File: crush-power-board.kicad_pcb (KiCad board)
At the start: 4 copper layers, 105 parts, among them J1 XT90PW-F, J2 1x2 Header, J3 Molex Micro Fit 3.0, J4 Barrel_Jack, J5 2157601008, U1 BD9G341AEFJ, U2 SIC461ED-T1-GE3, U3 SIC461ED-T1-GE3, U4 BD9G341AEFJ

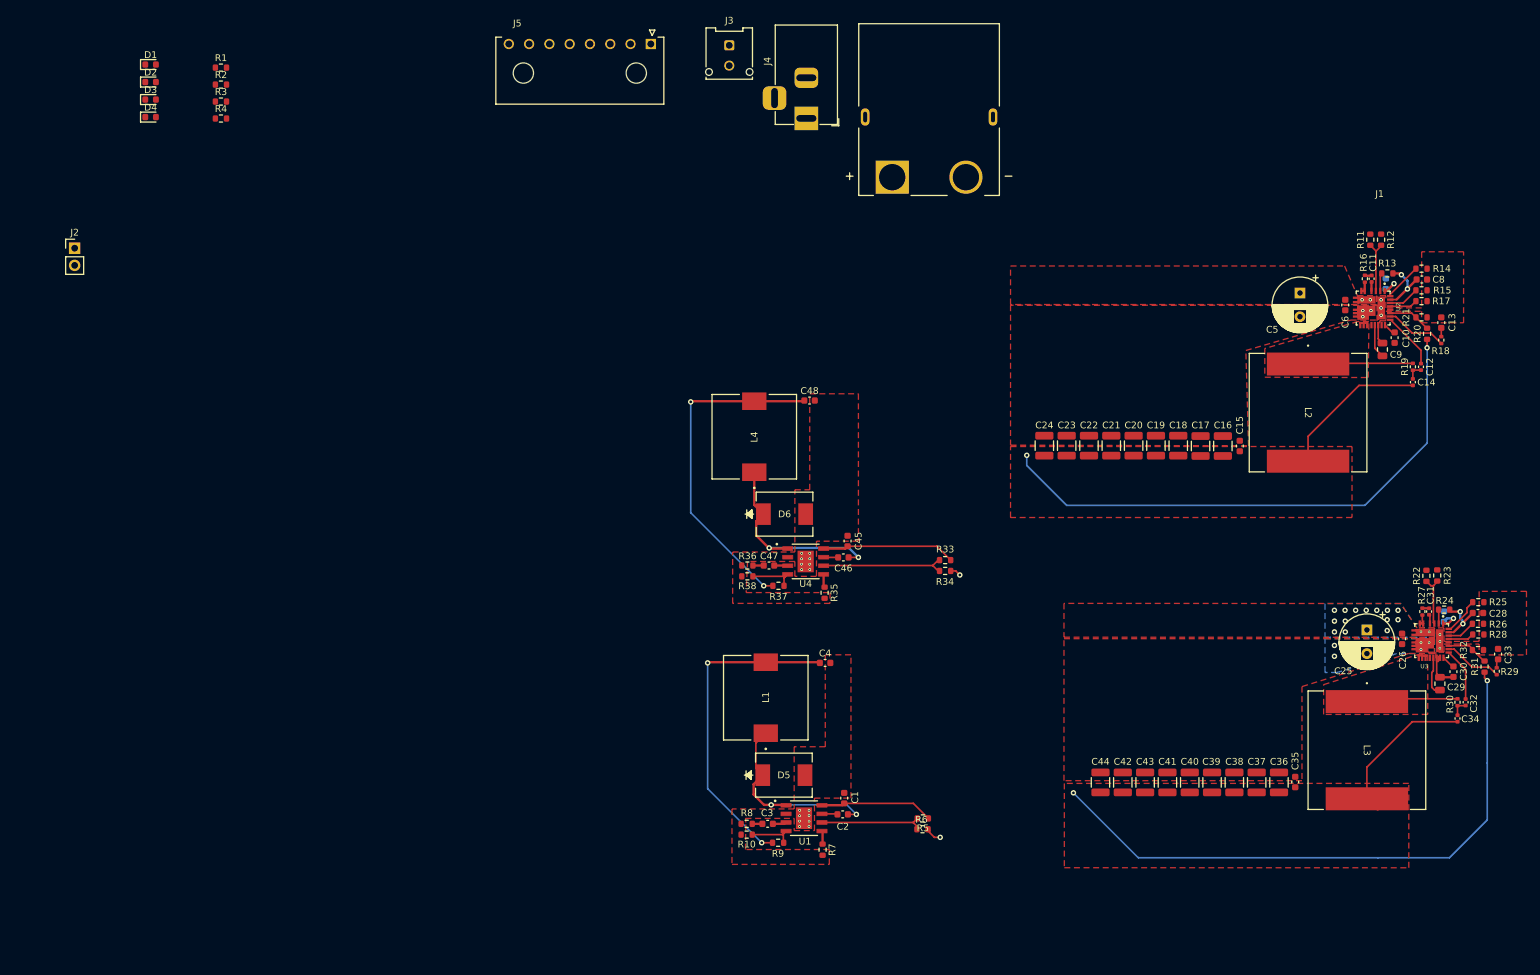
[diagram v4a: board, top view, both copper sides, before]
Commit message: fix drc violations
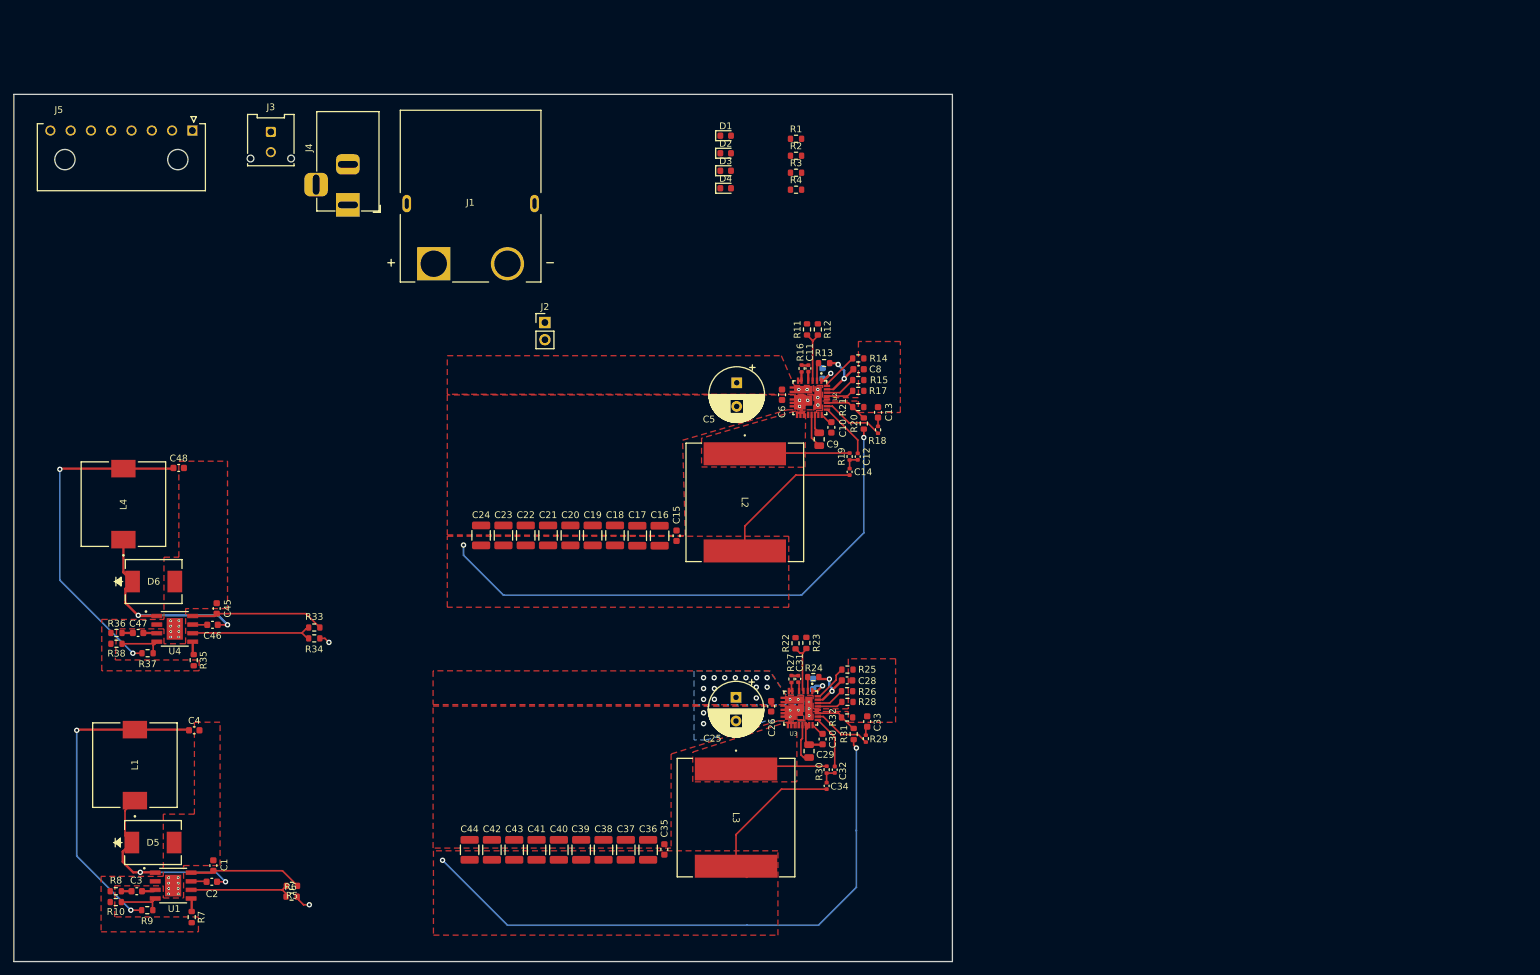
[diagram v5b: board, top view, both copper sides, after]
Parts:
- moved C2 93.8 mm to (71.0, 139.8)
- moved C25 93.8 mm to (148.5, 112.5)
- moved C26 93.8 mm to (153.7, 113.8)
- moved C28 93.8 mm to (164.9, 110.0)
- moved C3 93.8 mm to (59.9, 141.2)
- moved C31 93.8 mm to (157.7, 109.8)
- moved C36 93.8 mm to (135.5, 135.1)
- moved C37 93.8 mm to (132.2, 135.1)
- moved C39 93.8 mm to (125.6, 135.1)
- moved C4 93.8 mm to (68.4, 117.4)
- moved C41 93.8 mm to (119.0, 135.1)
- moved C44 93.8 mm to (109.1, 135.1)
- moved D6 93.8 mm to (62.4, 95.4)
- moved L1 93.8 mm to (59.6, 122.5)
- moved L3 93.8 mm to (148.5, 130.3)
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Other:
- board outline added: 138.8 x 128.2 mm

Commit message: preparing for board layout
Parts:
- moved R1 115.1 mm to (42.4, 33.4)
- moved R2 115.1 mm to (42.4, 35.9)
- moved R3 115.1 mm to (42.4, 38.4)
- moved R4 115.1 mm to (42.4, 40.9)
- moved D4 97.6 mm to (50.1, 25.8)
- moved D1 94.0 mm to (53.1, 33.2)
- moved D2 94.0 mm to (53.1, 35.8)
- moved D3 94.0 mm to (53.1, 38.4)
- moved C15 69.7 mm to (73.5, 66.8), turned to 0 degrees
- moved C16 68.1 mm to (73.5, 64.3), turned to 0 degrees
- moved J2 67.6 mm to (67.2, 15.2)
- moved C35 67.4 mm to (73.1, 116.7), turned to 0 degrees
- moved R22 66.7 mm to (92.7, 88.1), turned to 180 degrees
- moved C7 66.6 mm to (97.6, 45.1), turned to 0 degrees
- moved R23 66.6 mm to (95.0, 85.9)
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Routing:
- net 12V: track 104.6 -> 118.4 mm
- net 5V: track 112.9 -> 121.2 mm
- net Net-(U3-EN): track 7.77 -> 12.0 mm
- net GND1: track 1.60 -> 0.00 mm, vias 9 -> 8
- net +BATT: track 24.0 -> 25.3 mm
- net GND: track 10.7 -> 9.65 mm, vias 27 -> 92
- added copper zone on In2.Cu, net GND
- removed copper zone on B.Cu, net +BATT
- removed copper zone on B.Cu, net GND
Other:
- board size 138.8 x 128.2 mm -> 101.4 x 120.3 mm

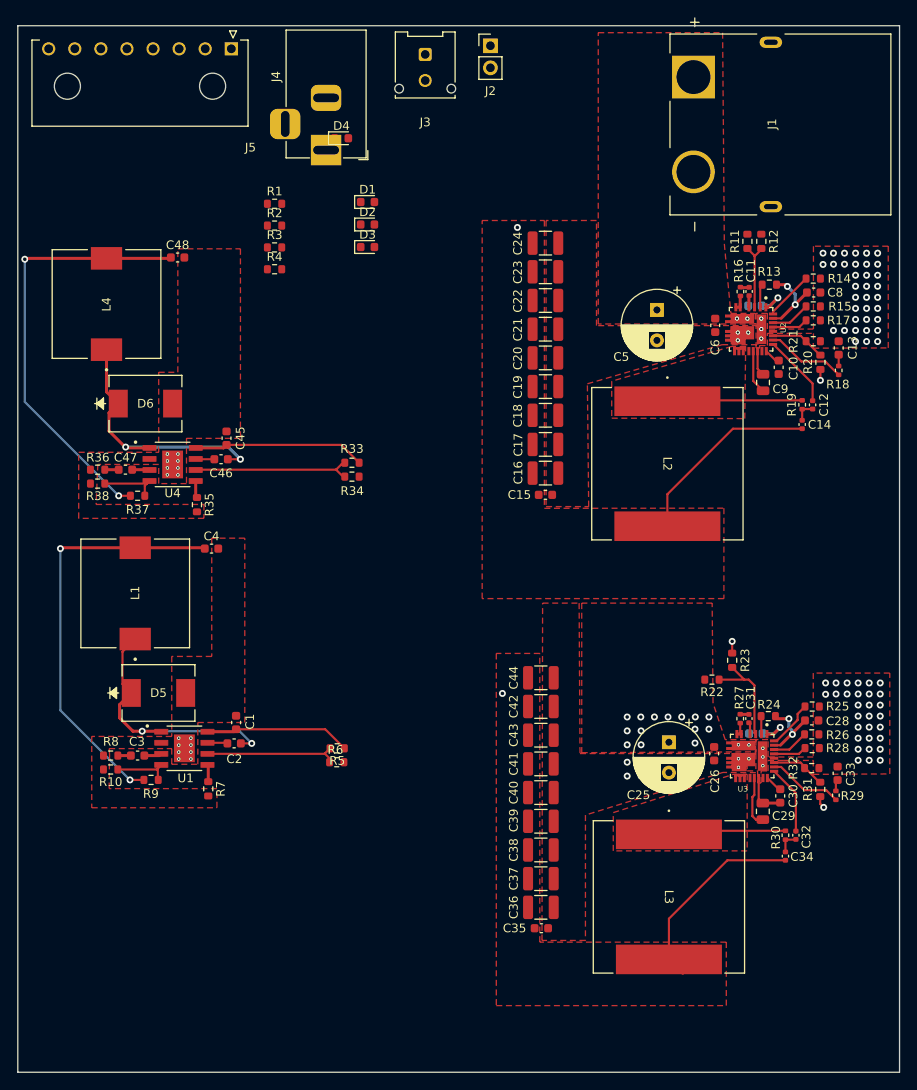
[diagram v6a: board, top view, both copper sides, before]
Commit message: layout majority of power board
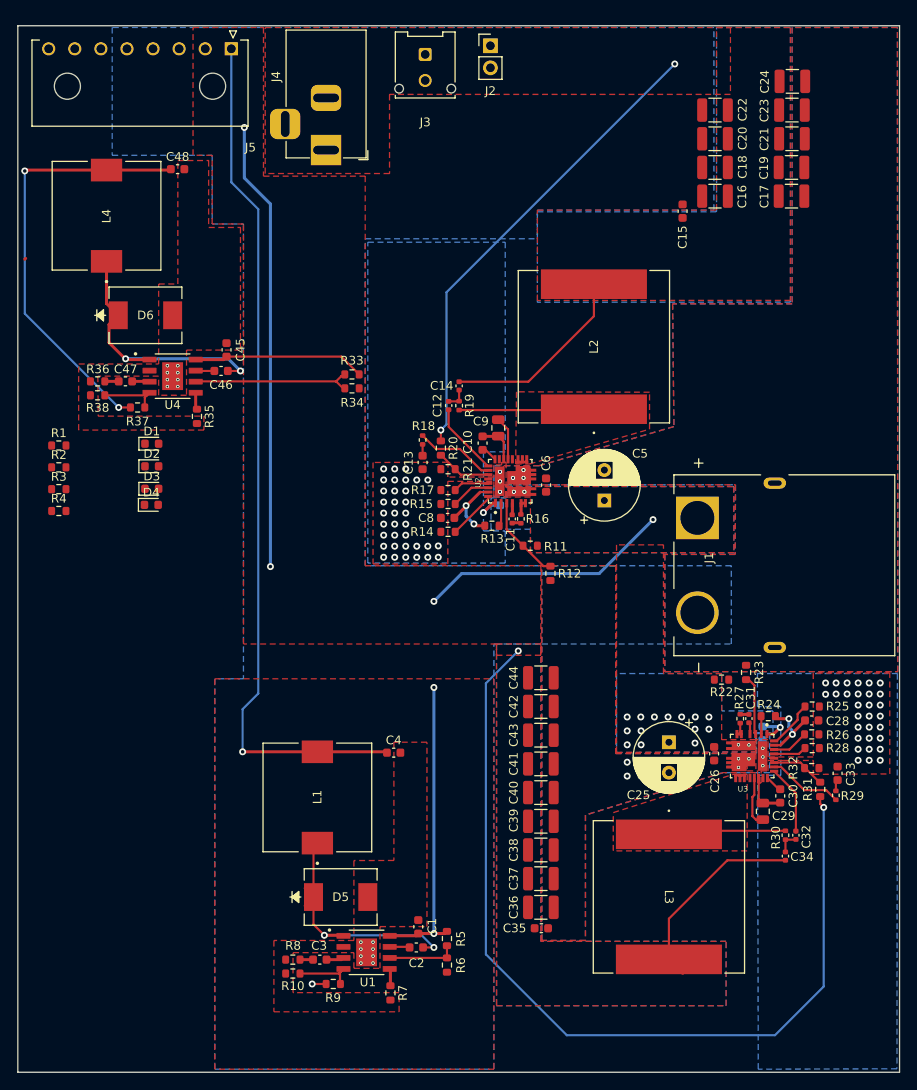
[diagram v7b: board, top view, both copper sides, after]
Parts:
- moved R14 51.1 mm to (62.3, 71.1), turned to 180 degrees
- moved J1 50.7 mm to (99.9, 75.0)
- moved C13 49.6 mm to (59.4, 63.1), turned to -90 degrees
- moved C8 49.4 mm to (62.3, 69.5), turned to 0 degrees
- moved R18 48.5 mm to (59.4, 60.5), turned to -90 degrees
- moved R15 47.8 mm to (62.3, 67.9), turned to 180 degrees
- moved D4 47.5 mm to (28.2, 68.0)
- moved R17 46.3 mm to (62.3, 66.3), turned to 180 degrees
- moved R12 45.2 mm to (74.1, 75.9), turned to 90 degrees
- moved R20 44.8 mm to (61.5, 61.5), turned to -90 degrees
- moved R21 44.5 mm to (62.3, 63.9), turned to 180 degrees
- moved R11 43.0 mm to (71.8, 72.7), turned to 0 degrees
- moved R13 42.3 mm to (67.4, 70.4), turned to 0 degrees
- moved C12 41.9 mm to (62.4, 56.6), turned to 90 degrees
- moved C17 40.2 mm to (101.8, 32.5)
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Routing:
- net +BATT: track 25.3 -> 167.9 mm, vias 20 -> 26
- net 3V3: track 48.5 -> 131.1 mm
- net 12V: track 118.4 -> 76.8 mm
- net Net-(U1-EN): track 15.6 -> 7.99 mm
- net 5V: track 121.2 -> 126.9 mm
- net Net-(U3-EN): track 12.0 -> 7.10 mm
- net Net-(U2-EN): track 8.31 -> 9.80 mm
- net Net-(D5-K): track 32.0 -> 30.8 mm
- net GND: track 9.65 -> 9.83 mm, vias 92 -> 91
- added copper zone on B.Cu, net +BATT
- added copper zone on B.Cu, net 12V
- added copper zone on B.Cu, net 5V
- added copper zone on B.Cu, net GND

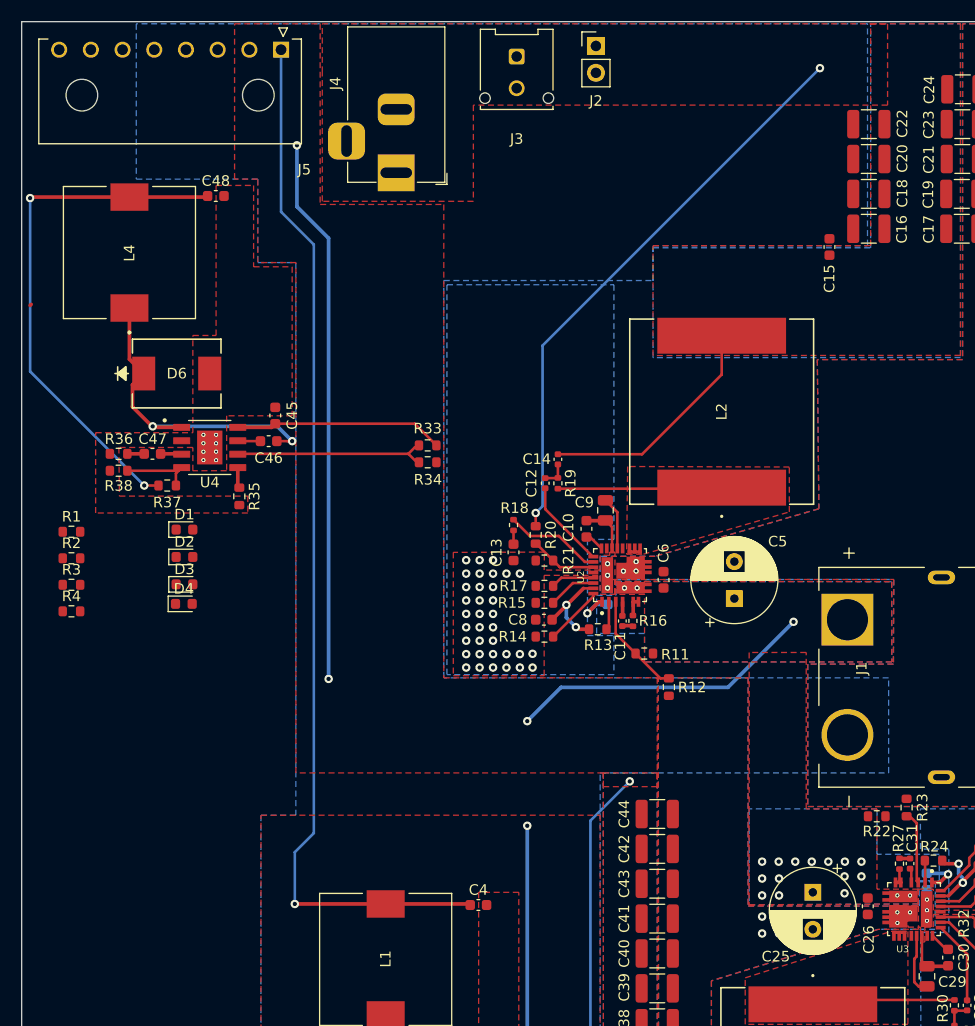
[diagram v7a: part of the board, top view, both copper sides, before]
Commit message: drc fixes and update schematic to reflect correct ic footprints
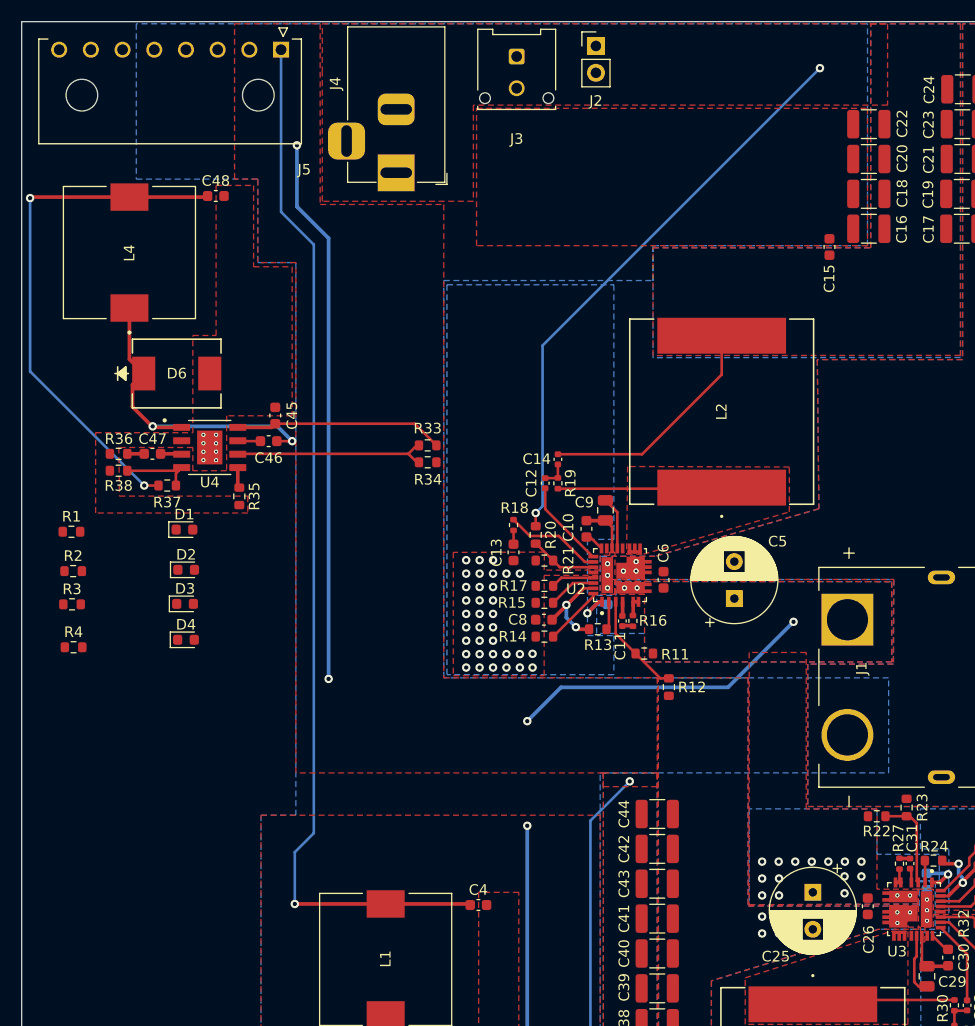
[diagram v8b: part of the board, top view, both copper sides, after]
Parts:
- moved D4 3.41 mm to (28.4, 71.4)
- moved R4 3.41 mm to (17.8, 72.1)
- moved D3 1.85 mm to (28.3, 68.0)
- moved R3 1.85 mm to (17.6, 68.0)
- moved R2 1.23 mm to (17.7, 64.9)
- moved D2 1.23 mm to (28.4, 64.8)
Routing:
- net Net-(U3-EN): track 7.10 -> 8.90 mm
